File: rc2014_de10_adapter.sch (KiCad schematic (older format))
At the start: 39 parts, among them J1 Conn_02x20_Odd_Even, J2 Conn_01x10_Male, J3 Conn_01x08_Male, J4 Z80 Bus, J5 Pro Bus, J6 M3 Mounting Hole, J7 FTDI, U1 SN74LVC245A, U2 SN74LVC245A, U3 SN74LVC245A, U4 SN74LVC245A, U5 SN74LVC245A, U6 AZ1117-3.3, U7 MAX40200AUK, U8 MAX40200AUK

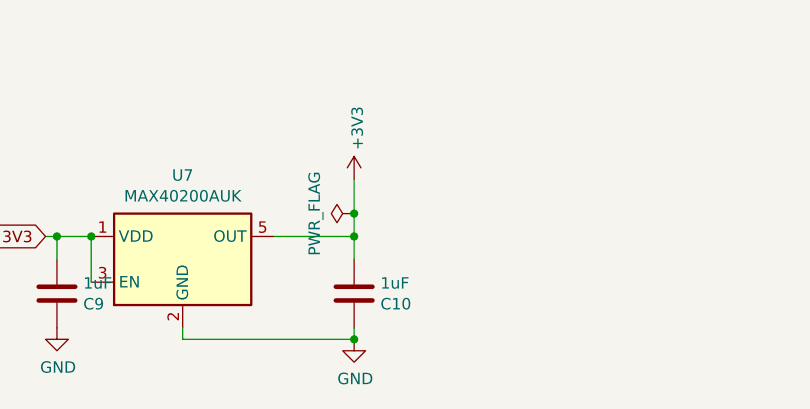
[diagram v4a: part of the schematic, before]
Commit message: fixed cap values
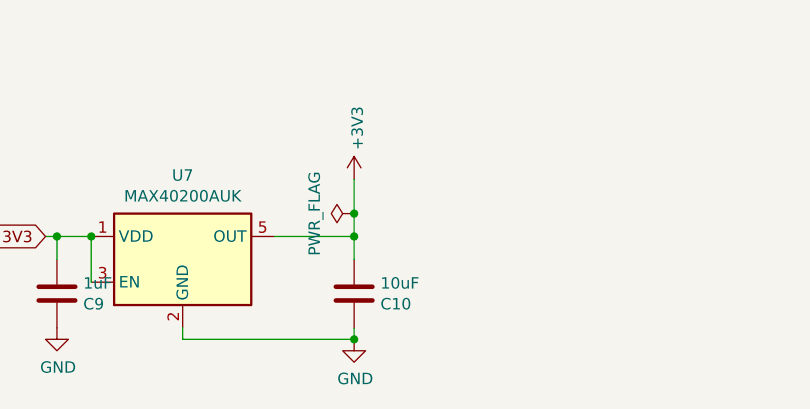
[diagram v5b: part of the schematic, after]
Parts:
- C10: value 1uF -> 10uF
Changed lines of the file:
@@
 P 4450 7300
 F 0 "C10" H 4565 7346 50  0000 L CNN
-F 1 "1uF" H 4565 7255 50  0000 L CNN
+F 1 "10uF" H 4565 7255 50  0000 L CNN
 F 2 "Capacitor_SMD:C_0805_2012Metric_Pad1.15x1.40mm_HandSolder" H 4488 7150 50  0001 C CNN
 F 3 "https://www.mouser.com/datasheet/2/212/KEM_C1002_X7R_SMD-1102033.pdf" H 4450 7300 50  0001 C CNN
